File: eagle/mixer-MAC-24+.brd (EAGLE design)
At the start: 34 x 24 mm, 10 parts, among them J1 142-0701-851, J2 142-0701-851, J3 142-0701-851, U1 MAC-24+

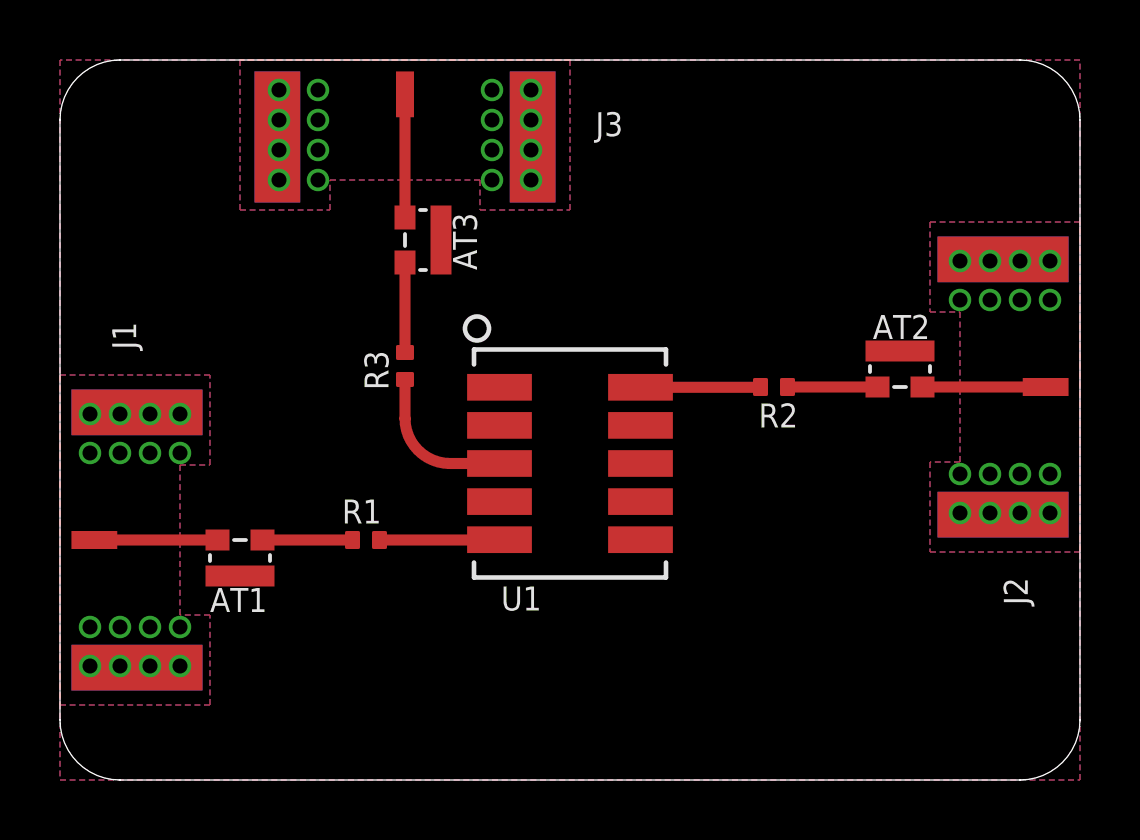
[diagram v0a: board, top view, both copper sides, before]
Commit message: Add stitching and finalize
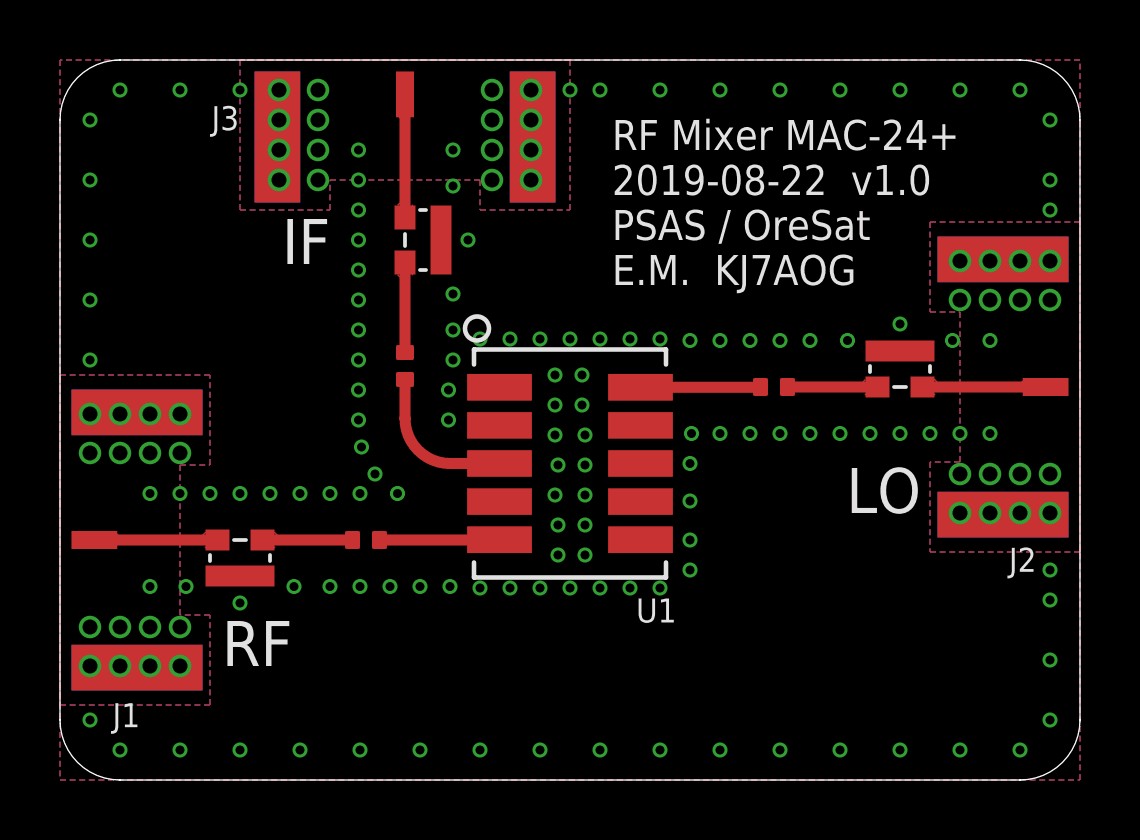
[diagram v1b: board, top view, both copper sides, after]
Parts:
- renumbered R1 to Z1, R2 to Z2, R3 to Z3
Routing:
- added copper zone on layer 1, net IF
- added copper zone on layer 1, net LO
- added copper zone on layer 1, net N$7
- added copper zone on layer 1, net N$8
- added copper zone on layer 1, net N$9
- added copper zone on layer 1, net RF
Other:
- board text added: "IF"
- board text added: "LO"
- board text added: "RF"
- board text added: "RF Mixer MAC-24+ 2019-08-22 v1.0 PSAS / OreSat E.M. KJ7AOG"
